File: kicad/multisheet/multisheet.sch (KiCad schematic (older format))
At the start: 2 parts

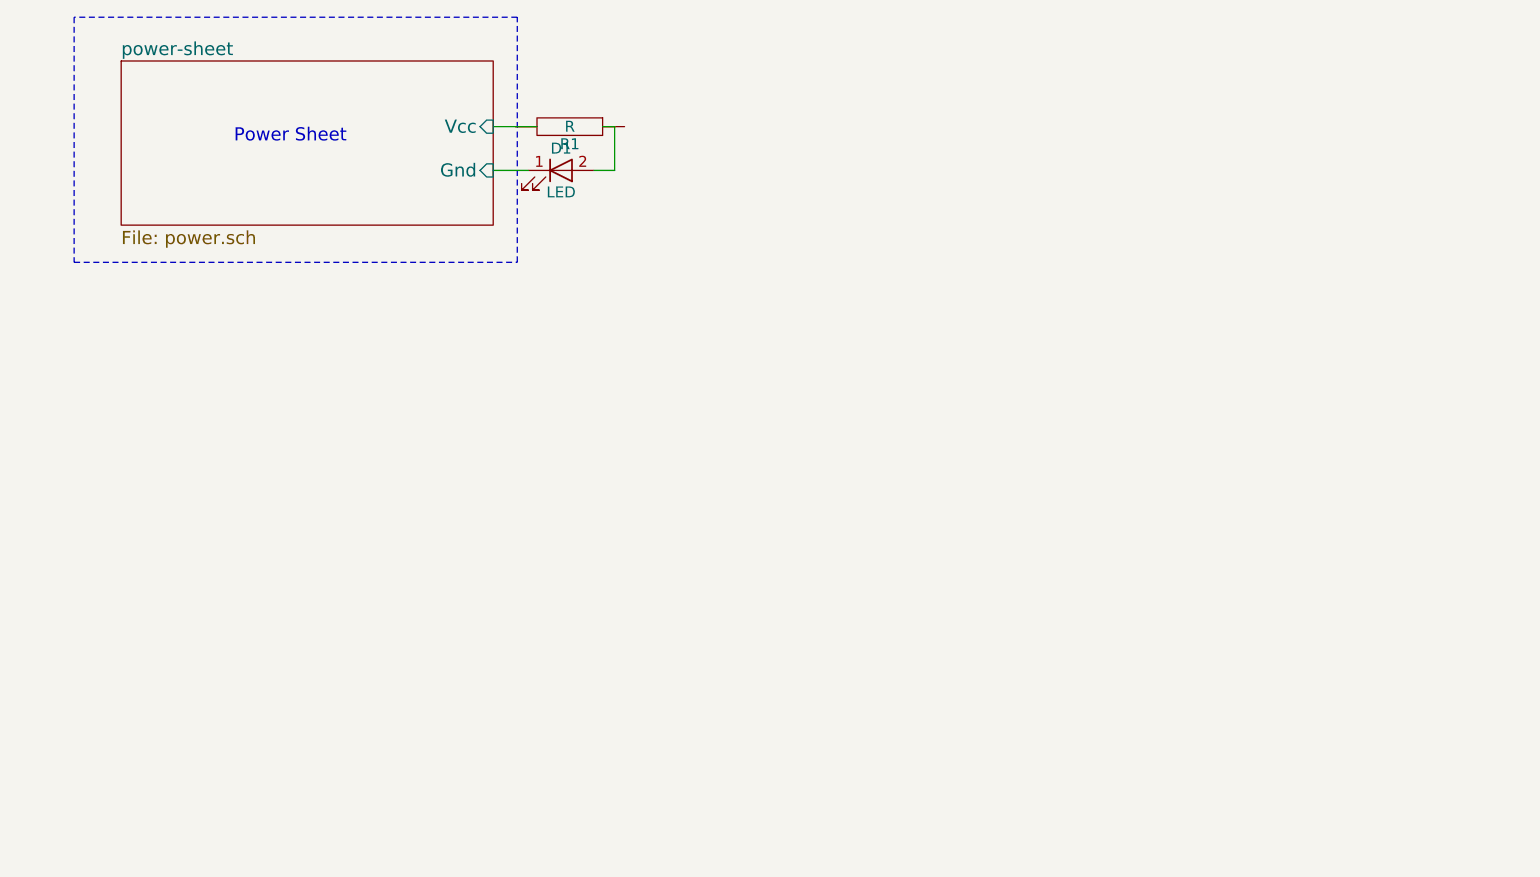
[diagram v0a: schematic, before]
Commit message: multisheet: Add stm32 sch imported from another project.
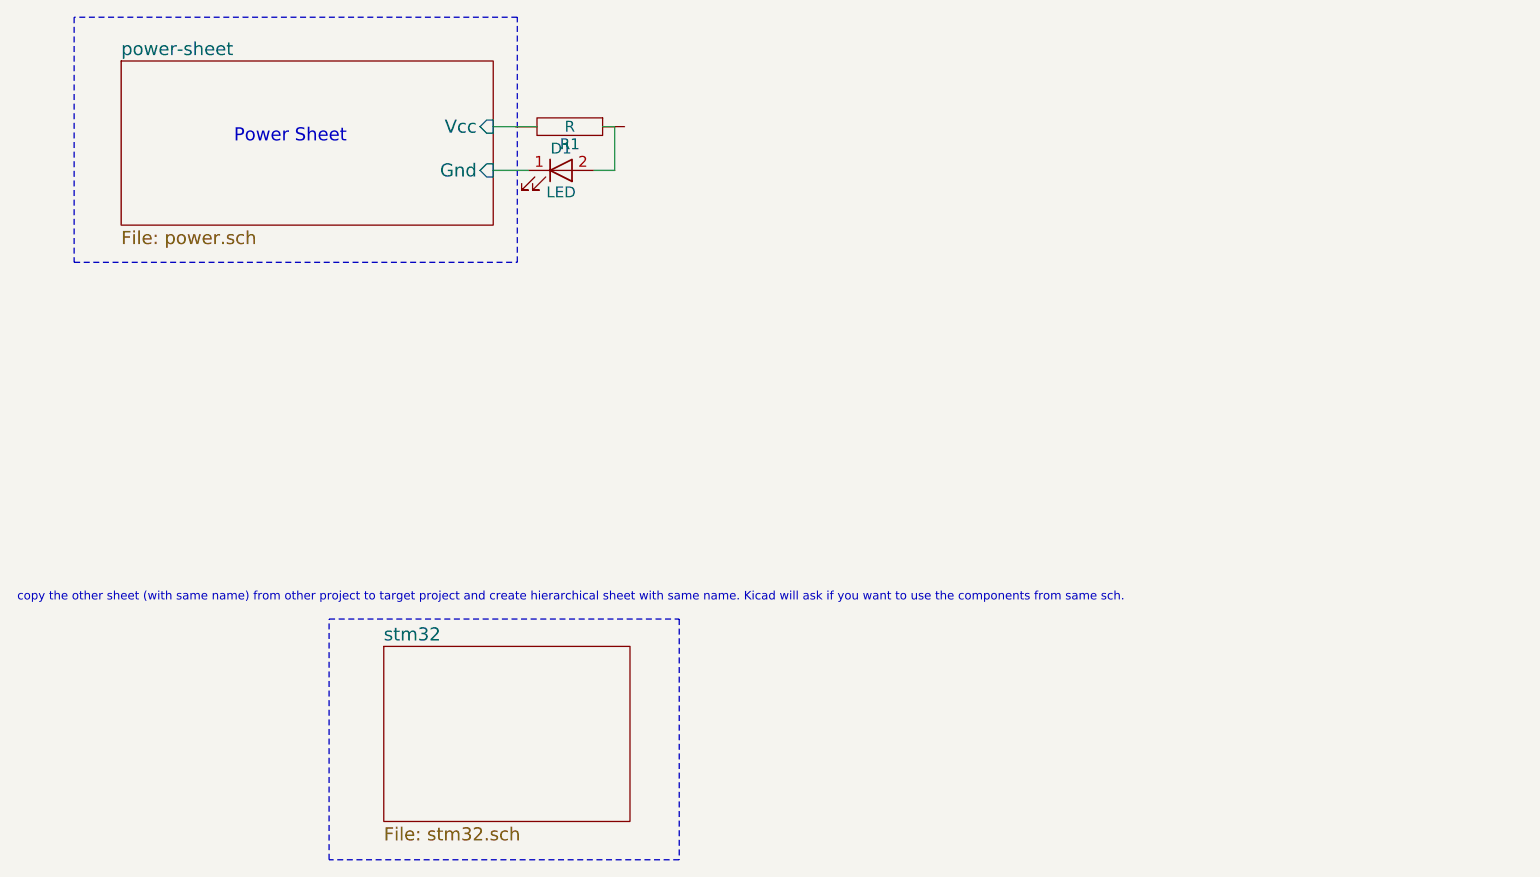
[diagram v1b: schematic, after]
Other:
- note added: "copy the other sheet (with same name) from other project to target project and create hierarchical sheet with same name. Kicad will ask if you want to use the components from same sch. \n"
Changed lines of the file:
@@
 EESchema Schematic File Version 2
+LIBS:Zilog
+LIBS:zetex
+LIBS:xilinx
+LIBS:Xicor
+LIBS:Worldsemi
+LIBS:wiznet
+LIBS:video
+LIBS:Valve
+LIBS:triac_thyristor
+LIBS:Transistor
+LIBS:Transformer
+LIBS:texas
+LIBS:Switch
+LIBS:supertex
+LIBS:siliconi
+LIBS:silabs
+LIBS:sensors
+LIBS:Sensor_Current
+LIBS:RFSolutions
+LIBS:rfcom
+LIBS:Relay
+LIBS:regul
+LIBS:references
+LIBS:pspice
+LIBS:Power_Management
+LIBS:powerint
 LIBS:power
+LIBS:philips
+LIBS:Oscillators
+LIBS:opto
+LIBS:onsemi
+LIBS:nxp
+LIBS:nordicsemi
+LIBS:motorola
+LIBS:motor_drivers
+LIBS:Motor
+LIBS:modules
+LIBS:microcontrollers
+LIBS:microchip
+LIBS:memory
+LIBS:Mechanical
+LIBS:MCU_Texas_MSP430
+LIBS:MCU_ST_STM32
+LIBS:MCU_ST_STM8
+LIBS:MCU_Parallax
+LIBS:MCU_NXP_S08
+LIBS:MCU_NXP_LPC
+LIBS:MCU_NXP_Kinetis
+LIBS:MCU_Microchip_PIC32
+LIBS:MCU_Microchip_PIC24
+LIBS:MCU_Microchip_PIC18
+LIBS:MCU_Microchip_PIC16
+LIBS:MCU_Microchip_PIC12
+LIBS:MCU_Microchip_PIC10
+LIBS:maxim
+LIBS:Logic_TTL_IEEE
+LIBS:logic_programmable
+LIBS:Logic_CMOS_IEEE
+LIBS:Logic_CMOS_4000
+LIBS:Logic_74xx
+LIBS:Logic_74xgxx
+LIBS:linear
+LIBS:LEM
+LIBS:LED
+LIBS:Lattice
+LIBS:ir
+LIBS:intersil
+LIBS:interface
+LIBS:intel
+LIBS:infineon
+LIBS:hc11
+LIBS:Graphic
+LIBS:gennum
+LIBS:ftdi
+LIBS:FPGA_Actel
+LIBS:Espressif
+LIBS:ESD_Protection
+LIBS:elec-unifil
+LIBS:DSP_Microchip_DSPIC33
+LIBS:dsp
+LIBS:driver_gate
+LIBS:Display
+LIBS:Diode
+LIBS:digital-audio
 LIBS:device
-LIBS:switches
-LIBS:relays
-LIBS:motors
-LIBS:transistors
-LIBS:conn
-LIBS:linear
-LIBS:regul
-LIBS:74xx
-LIBS:cmos4000
+LIBS:dc-dc
+LIBS:cypress
+LIBS:contrib
+LIBS:Connector
+LIBS:brooktre
+LIBS:Bosch
+LIBS:bbd
+LIBS:Battery_Management
+LIBS:audio
+LIBS:atmel
+LIBS:analog_switches
+LIBS:analog_devices
+LIBS:Altera
 LIBS:adc-dac
-LIBS:memory
-LIBS:xilinx
-LIBS:microcontrollers
-LIBS:dsp
-LIBS:microchip
-LIBS:analog_switches
-LIBS:motorola
-LIBS:texas
-LIBS:intel
-LIBS:audio
-LIBS:interface
-LIBS:digital-audio
-LIBS:philips
-LIBS:display
-LIBS:cypress
-LIBS:siliconi
-LIBS:opto
-LIBS:atmel
-LIBS:contrib
-LIBS:valves
+LIBS:ac-dc
 LIBS:multisheet-cache
 EELAYER 25 0
@@
 $Descr A4 11693 8268
 encoding utf-8
-Sheet 1 2
+Sheet 1 3
 Title "multisheet example"
 Date "2017-11-10"
@@
 Wire Notes Line
 	3010 950  985  950
+$Sheet
+S 2400 3825 1125 800
+U 5A0AE477
+F0 "stm32" 60
+F1 "stm32.sch" 60
+$EndSheet
+Text Notes 725  3625 0    39   ~ 0
+copy the other sheet (with same name) from other project to target project and create hierarchical sheet with same name. Kicad will ask if you want to use the components from same sch. \n
+Wire Notes Line
+	2150 3700 3750 3700
+Wire Notes Line
+	3750 3700 3750 4800
+Wire Notes Line
+	3750 4800 2150 4800
+Wire Notes Line
+	2150 4800 2150 3700
 $EndSCHEMATC
